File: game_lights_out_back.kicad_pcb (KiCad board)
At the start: 2 copper layers, 171 x 127.3 mm, 5 parts

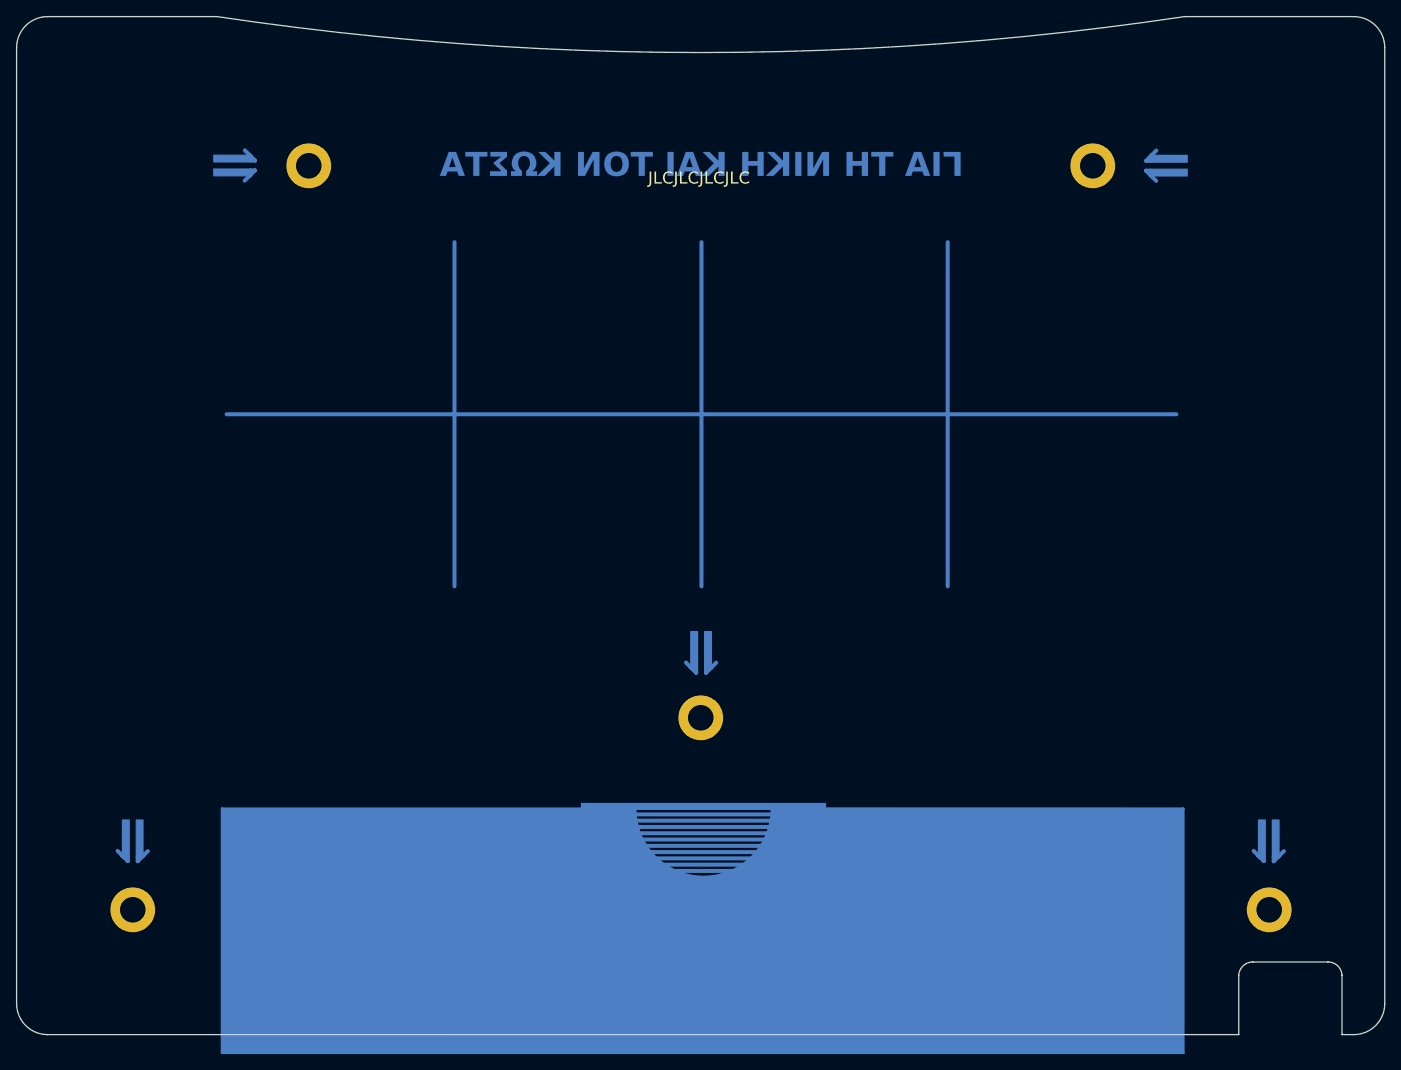
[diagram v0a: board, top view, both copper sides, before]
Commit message: Redesign to match the updated main board
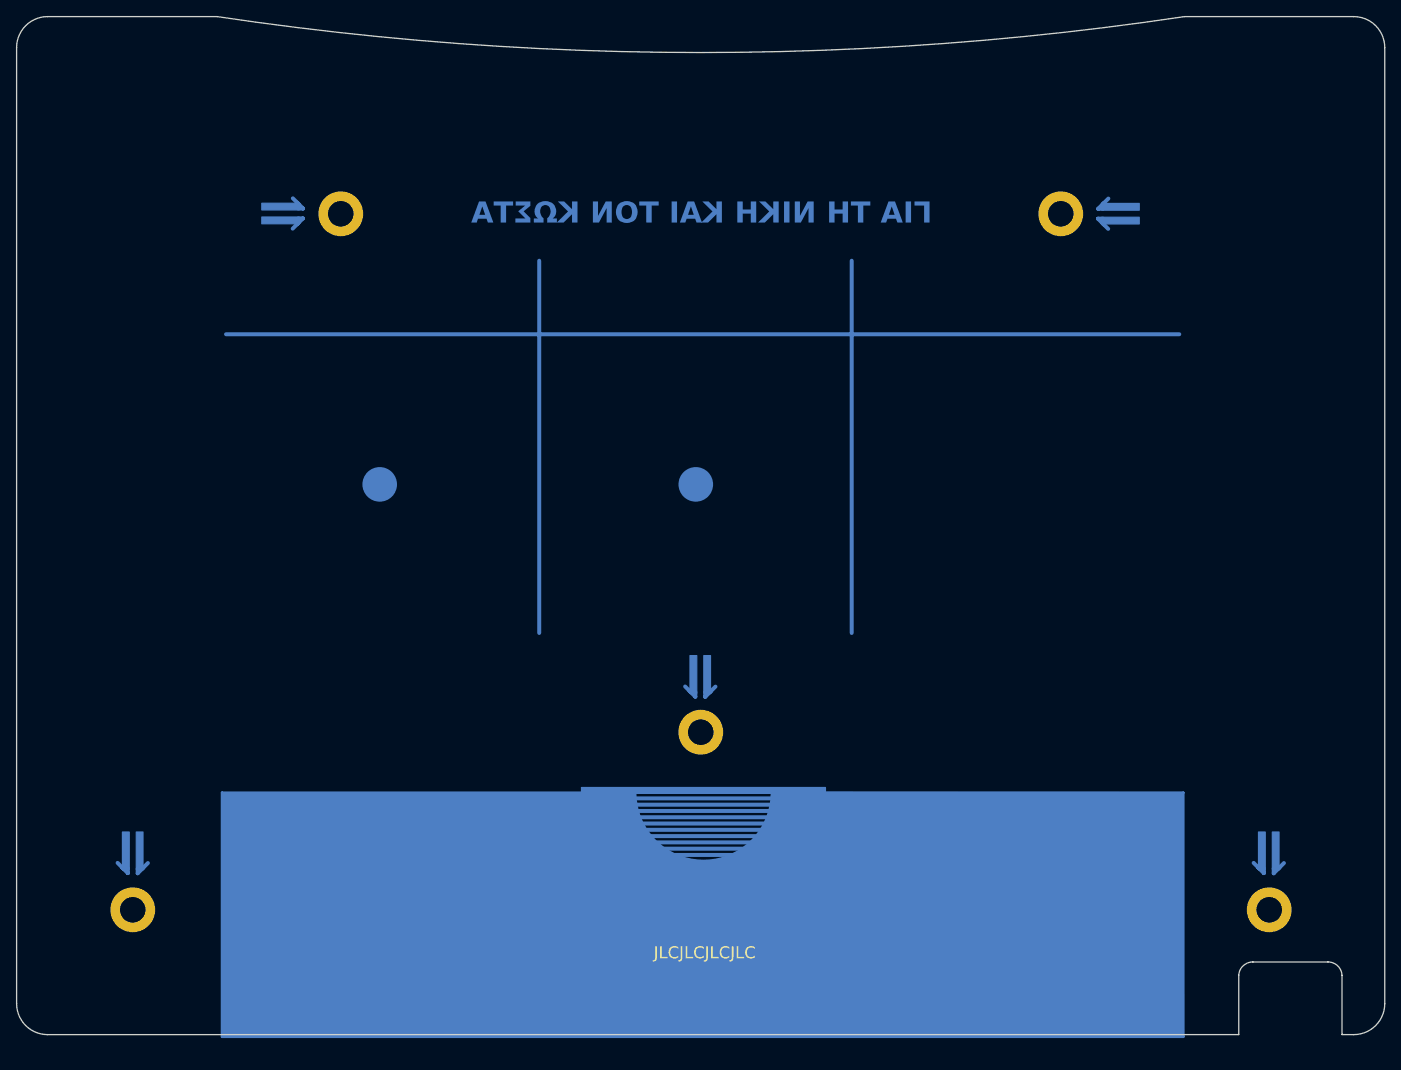
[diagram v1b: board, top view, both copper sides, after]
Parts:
- moved REF** 7.21 mm to (68.0, 61.0)
- moved REF** 7.21 mm to (158.0, 61.0)
- moved REF** 1.80 mm to (113.0, 125.8)
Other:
- board text added: "///"
- board text added: "Every configuration is solvable. Don't blame the game if you can't win ;)"
- board text added: "Fun facts:"
- board text added: "Marked lights will toggle when the middle one is pressed."
- board text added: "No key needs to be pressed more than once. It won't make any difference."
- board text removed: "MAD"
